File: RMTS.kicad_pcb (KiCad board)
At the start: 2 copper layers, 78.1 x 50.2 mm, 79 parts, among them J1 USB_B_Mini, J10 CONN_02, J11 CONN_02, J12 CONN_02, J2 Programmer, J3 Screw_Terminal_01x03, J4 Screw_Terminal_01x04, J5 Screw_Terminal_01x02, J6 Screw_Terminal_01x02, J7 Micro_SD_Card_Det_Hirose_DM3AT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

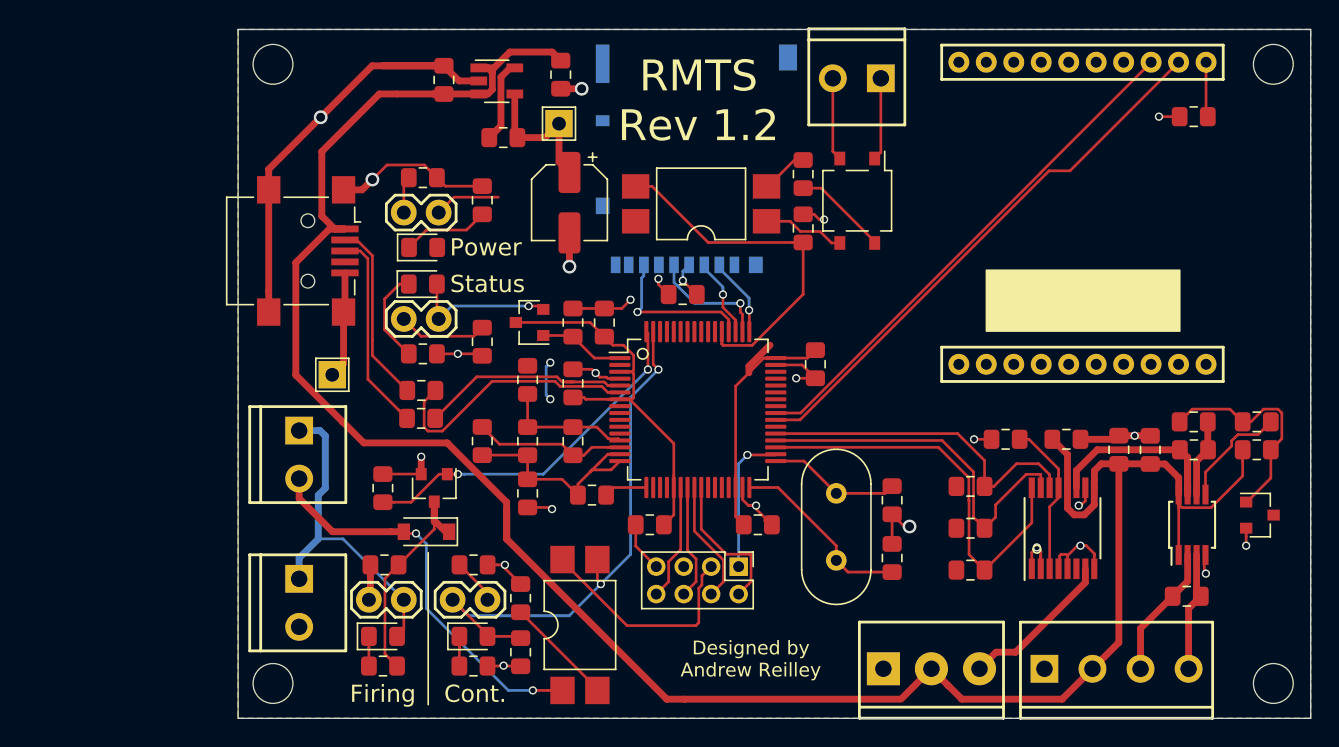
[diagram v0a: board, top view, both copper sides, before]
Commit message: Update programmer header, remove USB port
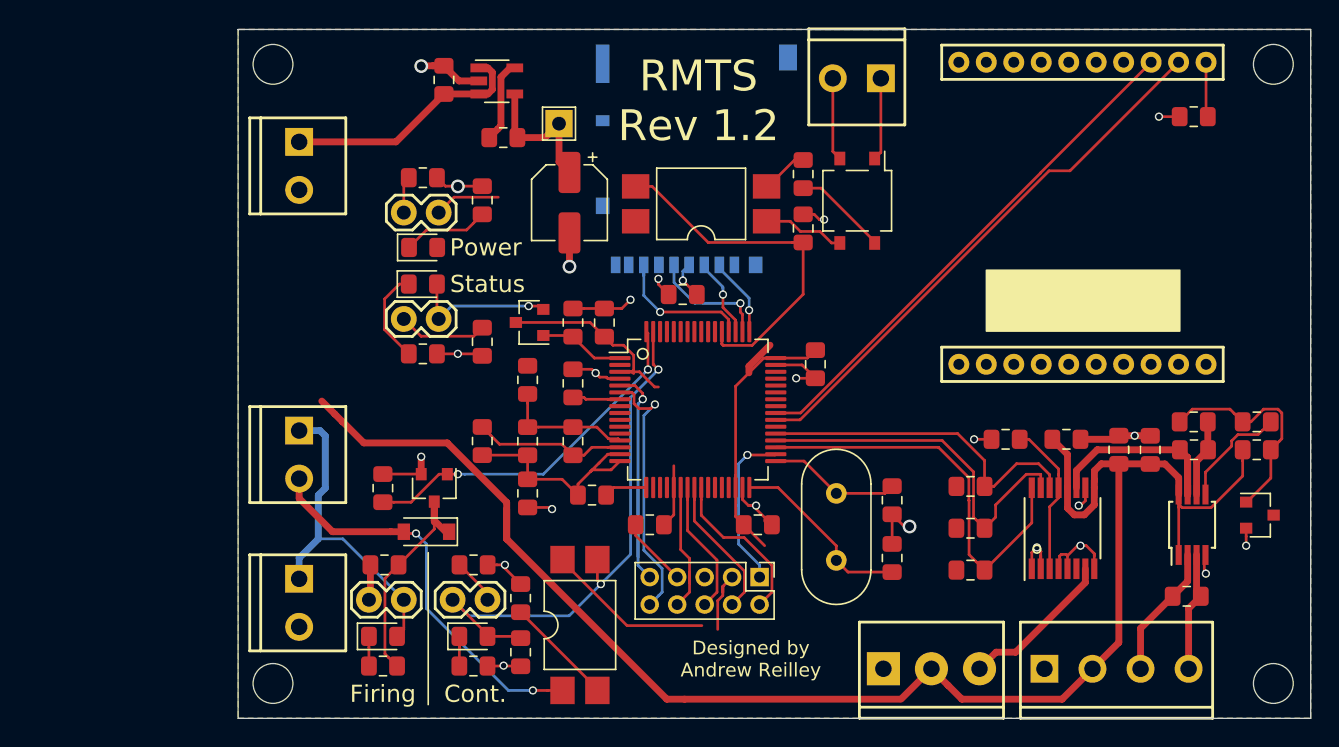
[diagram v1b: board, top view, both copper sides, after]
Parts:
- removed R1, R2: 33, Resistor_SMD:R_0805_2012Metric_Pad1.15x1.40mm_HandSolder
- removed R13: 330, Resistor_SMD:R_0805_2012Metric_Pad1.15x1.40mm_HandSolder
- removed TP1: GND, TestPoint:TestPoint_THTPad_2.0x2.0mm_Drill1.0mm
- J1: value USB_B_Mini -> Screw_Terminal_01x02; footprint Connector_USB:USB_Mini-B_Lumberg_2486_01_Horizontal -> Connectors:SCREWTERMINAL-3.5MM-2
- J2: footprint Connector_PinHeader_2.00mm:PinHeader_2x04_P2.00mm_Vertical -> Connector_PinHeader_2.00mm:PinHeader_2x05_P2.00mm_Vertical
- moved J1 7.97 mm to (136.5, 70.4)
- moved J2 1.70 mm to (170.1, 102.1)
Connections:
- C1 pad 1: /VBUS -> Net-(C1-Pad1)
- J1 pad 1: /VBUS -> Net-(C1-Pad1)
- J1 pad 2: Net-(J1-Pad2) -> GND
- U1 pad 1: /VBUS -> Net-(C1-Pad1)
- U1 pad 3: /VBUS -> Net-(C1-Pad1)
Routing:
- net /VBUS: track 165.2 -> 118.3 mm
- net GND: track 123.5 -> 78.6 mm, vias 24 -> 23
- net Net-(C1-Pad1): track 0.00 -> 18.0 mm
- net Net-(J1-Pad3): track 14.7 -> 0.00 mm
- net Net-(J1-Pad2): track 13.3 -> 0.00 mm
- net +3V3: track 102.9 -> 96.8 mm, vias 3 -> 1
- net /USBP: track 15.6 -> 20.8 mm, vias 0 -> 1
- net /PTA0: track 8.50 -> 9.96 mm
- net /RST: track 10.5 -> 11.9 mm
- net /PTA2: track 9.01 -> 10.4 mm
- net /PTA1: track 8.39 -> 9.79 mm
- net /PTA3: track 10.7 -> 11.9 mm
- net /SD_DO: track 11.4 -> 10.8 mm
- net /USBM: track 19.2 -> 19.4 mm, vias 0 -> 1

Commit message: Added 5v reg, broke layout
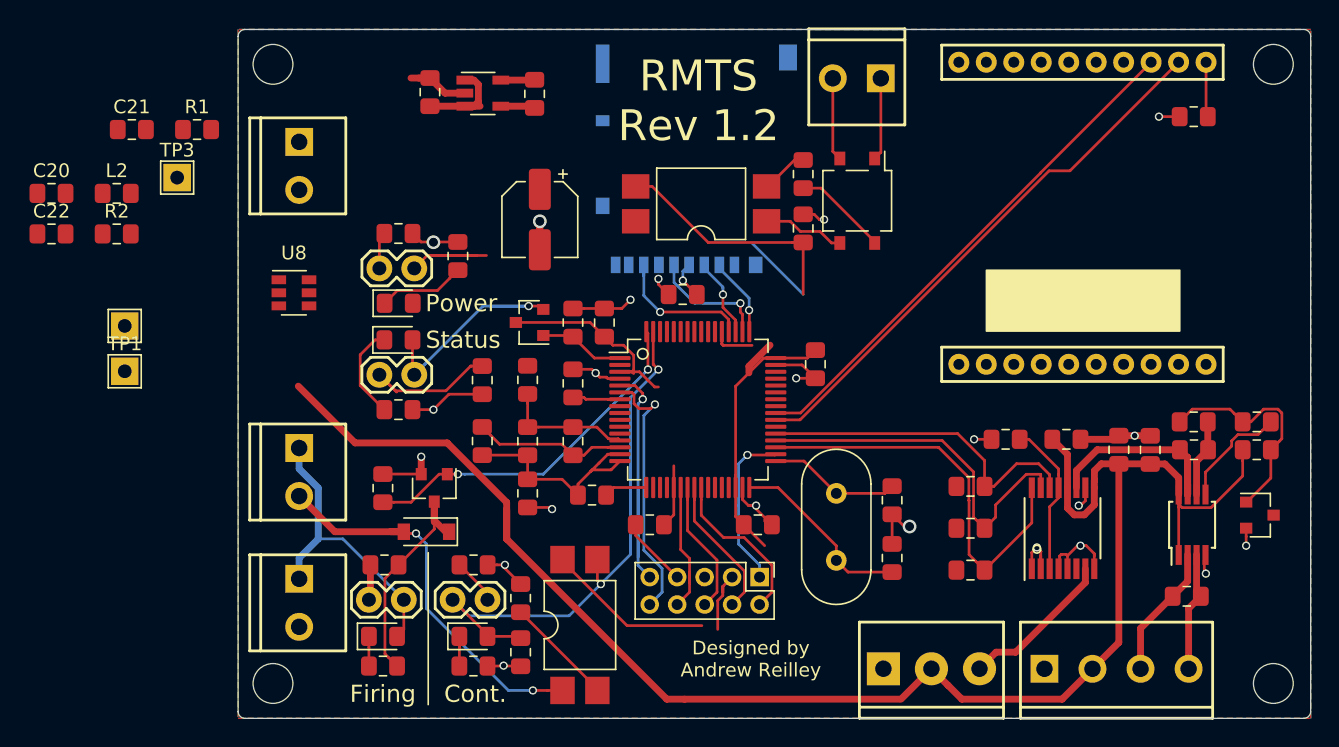
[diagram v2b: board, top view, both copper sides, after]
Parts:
- added C20: 2.2uF, Capacitor_SMD:C_0805_2012Metric_Pad1.15x1.40mm_HandSolder, F.Cu at (118.5, 74.2)
- added C21: 0.1uF, Capacitor_SMD:C_0805_2012Metric_Pad1.15x1.40mm_HandSolder, F.Cu at (124.3, 69.5)
- added C22: 10uF, Capacitor_SMD:C_0805_2012Metric_Pad1.15x1.40mm_HandSolder, F.Cu at (118.5, 77.1)
- added L2: 4.7uH, Inductor_SMD:L_0805_2012Metric_Pad1.15x1.40mm_HandSolder, F.Cu at (123.2, 74.2)
- added R1: 88.7k, Resistor_SMD:R_0805_2012Metric_Pad1.15x1.40mm_HandSolder, F.Cu at (129.1, 69.5)
- added R2: 22.1k, Resistor_SMD:R_0805_2012Metric_Pad1.15x1.40mm_HandSolder, F.Cu at (123.2, 77.1)
- added TP1: GND, TestPoint:TestPoint_THTPad_2.0x2.0mm_Drill1.0mm, F.Cu at (123.8, 87.1)
- added TP3: 5V, TestPoint:TestPoint_THTPad_2.0x2.0mm_Drill1.0mm, F.Cu at (127.6, 73.0)
- added U8: LMR50410-Q1, Package_TO_SOT_SMD:SOT-23-6, F.Cu at (136.1, 81.4)
- moved TP2 34.9 mm to (123.8, 83.8)
- moved J11 4.44 mm to (144.9, 79.6)
- moved J12 4.44 mm to (144.9, 87.4)
- moved R16 4.44 mm to (148.1, 78.7)
- moved D5 4.44 mm to (143.8, 82.2)
- moved D6 4.44 mm to (143.8, 84.8)
- moved R17 4.44 mm to (143.8, 89.9)
- moved R19 4.44 mm to (143.8, 77.1)
- moved L1 3.91 mm to (153.7, 66.9), turned to 270 degrees
- moved R21 2.79 mm to (149.9, 87.8)
- moved C2 2.48 mm to (154.1, 76.1)
- moved C1 1.35 mm to (146.1, 66.8)
- moved U1 1.35 mm to (149.9, 66.9)
- moved J6 1.27 mm to (136.5, 92.7)
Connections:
- C1 pad 1: Net-(C1-Pad1) -> +5V
- C11 pad 1: /VBUS -> +5V
- C18 pad 1: /VBUS -> +5V
- C19 pad 1: /VBUS -> +5V
- J1 pad 1: Net-(C1-Pad1) -> Net-(C20-Pad1)
- J3 pad 2: /VBUS -> +5V
- J4 pad 2: /VBUS -> +5V
- R25 pad 1: /VBUS -> +5V
- U1 pad 1: Net-(C1-Pad1) -> +5V
- U1 pad 3: Net-(C1-Pad1) -> +5V
- U3 pad 10: GND -> Net-(U3-Pad10)
- U3 pad 12: /VBUS -> +5V
- U3 pad 9: /VBUS -> +5V
- U4 pad 1: /VBUS -> +5V
- U4 pad 8: /VBUS -> +5V
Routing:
- net +5V: track 0.00 -> 127.7 mm
- net /VBUS: track 118.3 -> 0.00 mm
- net Net-(C1-Pad1): track 18.0 -> 0.00 mm
- net Net-(D6-Pad2): track 10.9 -> 18.5 mm
- net GND: track 78.6 -> 84.3 mm, vias 23 -> 21
- net /EXT_FIRE: track 26.1 -> 20.8 mm
- net Net-(J12-Pad2): track 6.49 -> 10.5 mm
- net +3V3: track 96.8 -> 93.2 mm
- net Net-(L1-Pad1): track 6.04 -> 2.81 mm
- net Net-(D1-Pad2): track 26.2 -> 23.6 mm
- net Net-(U3-Pad10): track 0.00 -> 1.58 mm, vias 0 -> 1
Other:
- outline, holes or cut-outs redrawn

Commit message: Fixed layout of new 5v regulator
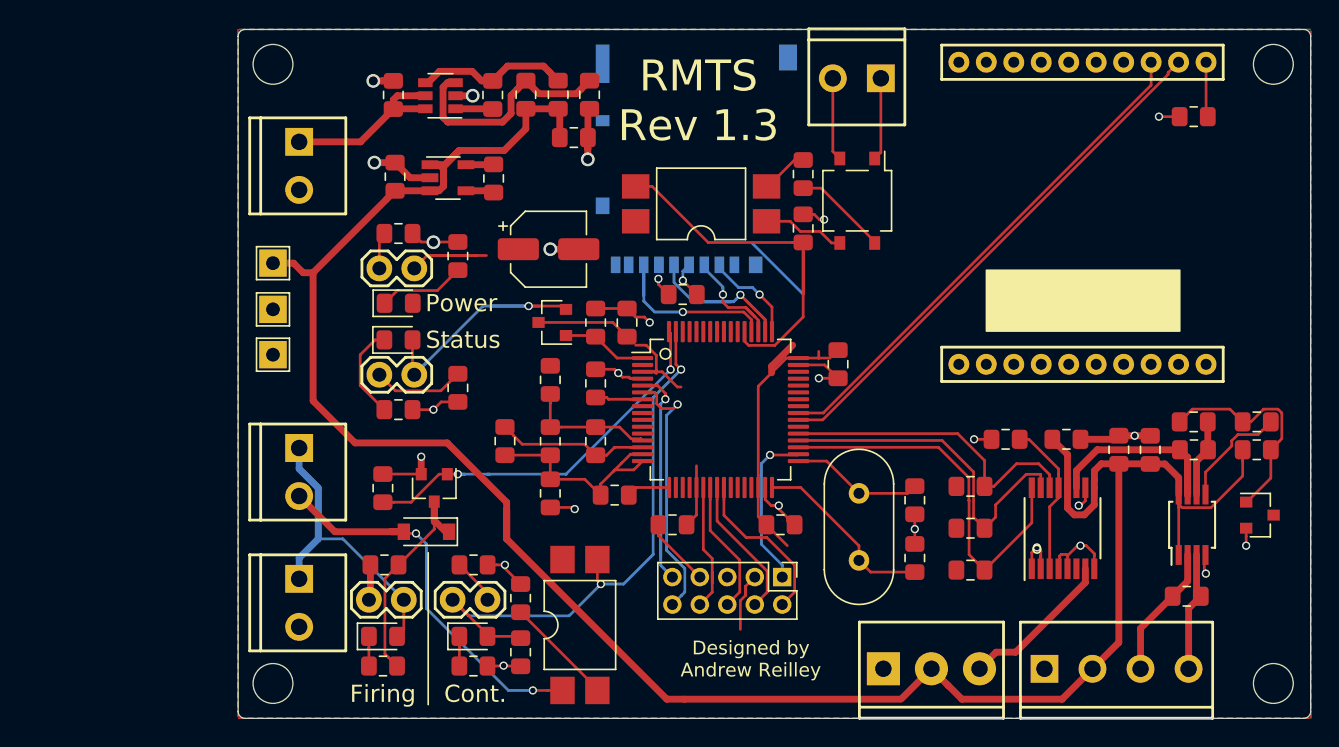
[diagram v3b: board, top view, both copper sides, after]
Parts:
- moved C22 38.7 mm to (156.5, 70.1)
- moved R2 35.9 mm to (157.7, 67.0), turned to 270 degrees
- moved L2 32.9 mm to (155.4, 67.0), turned to 270 degrees
- moved C21 26.4 mm to (150.6, 67.0), turned to 90 degrees
- moved C20 25.9 mm to (143.4, 67.0), turned to 90 degrees
- moved R1 24.1 mm to (153.0, 67.0), turned to 90 degrees
- moved U8 17.9 mm to (146.8, 67.1), turned to 180 degrees
- moved TP1 10.9 mm to (134.6, 85.9)
- moved TP2 10.9 mm to (134.6, 82.6)
- moved TP3 9.36 mm to (134.6, 79.2)
- moved L1 6.84 mm to (150.7, 73.1)
- moved U1 6.66 mm to (147.4, 73.0)
- moved C1 6.66 mm to (143.5, 73.0)
- moved C2 2.25 mm to (154.7, 78.2), turned to 0 degrees
- moved R21 1.86 mm to (148.1, 88.3)
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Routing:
- net +5V: track 127.7 -> 163.2 mm
- net Net-(R1-Pad2): track 0.00 -> 16.9 mm
- net Net-(C20-Pad1): track 0.00 -> 13.9 mm
- net +3V3: track 93.2 -> 79.7 mm
- net Net-(C21-Pad2): track 0.00 -> 11.2 mm
- net /SD_CLK: track 8.88 -> 17.7 mm
- net /EXT_FIRE: track 20.8 -> 28.4 mm
- net /SD_DO: track 10.8 -> 14.9 mm
- net Net-(J12-Pad2): track 10.5 -> 7.52 mm
- net Net-(C21-Pad1): track 0.00 -> 2.72 mm
- net Net-(D6-Pad2): track 18.5 -> 21.0 mm
- net /SD_DI: track 5.81 -> 8.18 mm
- net /Fire: track 26.1 -> 28.4 mm
- net GND: track 84.3 -> 86.4 mm, vias 21 -> 25
- net /ASDA: track 27.0 -> 25.3 mm
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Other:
- board text added: "RMTS Rev 1.3"
- board text removed: "RMTS Rev 1.2"

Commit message: Upgrade firing diode
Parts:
- D3: footprint Diode_SMD:D_SOD-123 -> Diode_SMD:D_SMA
- moved Q1 2.25 mm to (144.8, 94.0)
- moved R18 1.88 mm to (141.7, 94.0)
- moved D3 0.52 mm to (145.7, 98.3)
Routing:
- net Net-(D1-Pad2): track 23.6 -> 26.8 mm
- net /Fire: track 28.4 -> 30.8 mm
- net Net-(D3-Pad1): track 16.6 -> 18.5 mm
- net +5V: track 163.2 -> 161.5 mm
- net Net-(D3-Pad2): track 28.8 -> 27.8 mm
- net GND: track 86.4 -> 85.6 mm
- net +3V3: track 79.7 -> 78.9 mm

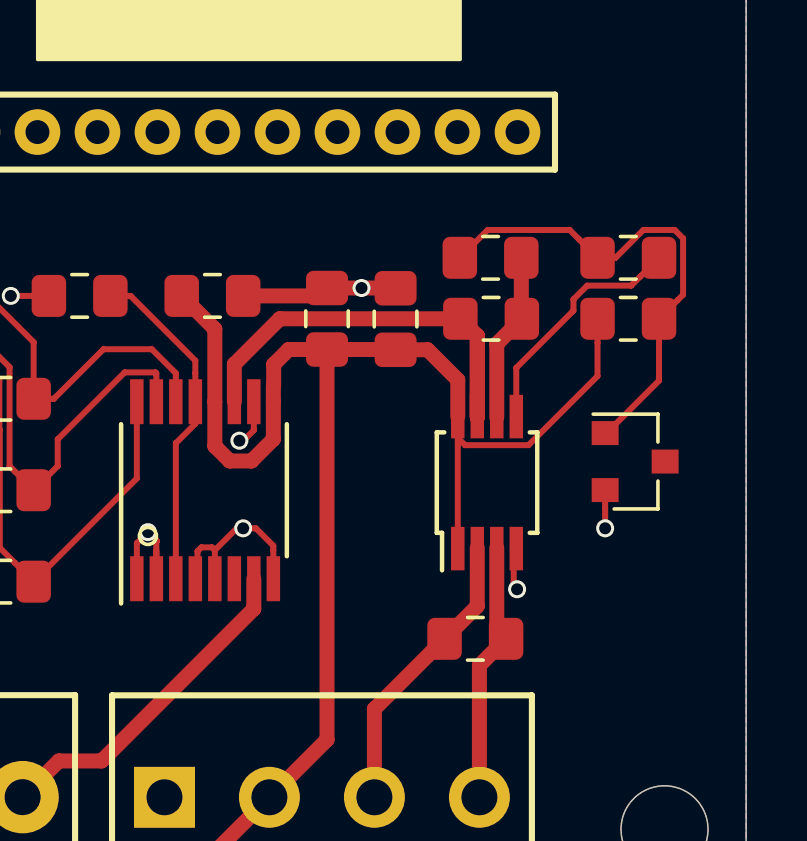
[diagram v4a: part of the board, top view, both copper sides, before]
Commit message: Added test points
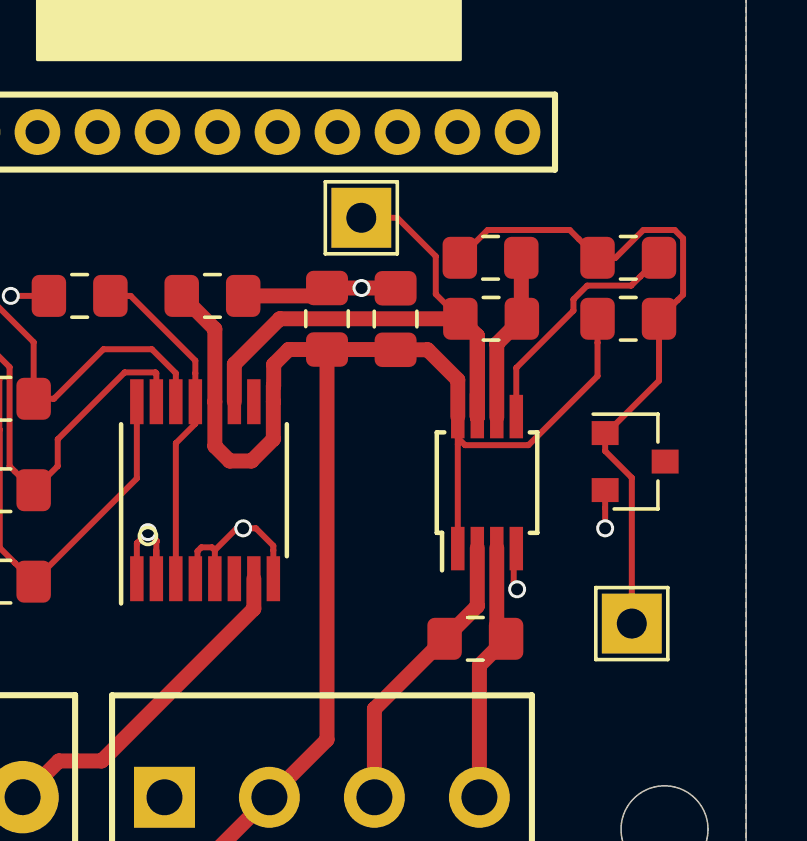
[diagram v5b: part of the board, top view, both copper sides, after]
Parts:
- added TP4: 5V, TestPoint:TestPoint_THTPad_2.0x2.0mm_Drill1.0mm, F.Cu at (206.4, 103.0)
- added TP5: 5V, TestPoint:TestPoint_THTPad_2.0x2.0mm_Drill1.0mm, F.Cu at (197.4, 89.5)
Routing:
- net Net-(R24-Pad2): track 16.3 -> 23.0 mm
- net /LC0: track 16.4 -> 21.8 mm
- net Net-(U3-Pad10): track 1.58 -> 0.00 mm, vias 1 -> 0
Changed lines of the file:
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@@
     (thickness 1.6)
     (drawings 33)
-    (tracks 652)
+    (tracks 656)
     (zones 0)
-    (modules 84)
+    (modules 86)
     (nets 111)
   )
@@
     (uvia_drill 0.1)
   )
+  (module TestPoint:TestPoint_THTPad_2.0x2.0mm_Drill1.0mm (layer F.Cu)
+    (at 197.358 89.4715)
+    (descr "THT rectangular pad as test Point, square 2.0mm_Drill1.0mm  side length, hole diameter 1.0mm")
+    (tags "test point THT pad rectangle square")
+    (attr virtual)
+    (fp_text reference TP5 (at -3.1115 0) (layer F.SilkS) hide
+      (effects (font (size 1 1) (thickness 0.15)))
+    )
+    (fp_text value 5V (at 0 2.05) (layer F.Fab)
+      (effects (font (size 1 1) (thickness 0.15)))
+    )
+    (fp_line (start 1.5 1.5) (end -1.5 1.5) (layer F.CrtYd) (width 0.05))
+    (fp_line (start 1.5 1.5) (end 1.5 -1.5) (layer F.CrtYd) (width 0.05))
+    (fp_line (start -1.5 -1.5) (end -1.5 1.5) (layer F.CrtYd) (width 0.05))
+    (fp_line (start -1.5 -1.5) (end 1.5 -1.5) (layer F.CrtYd) (width 0.05))
+    (fp_line (start -1.2 1.2) (end -1.2 -1.2) (layer F.SilkS) (width 0.12))
+    (fp_line (start 1.2 1.2) (end -1.2 1.2) (layer F.SilkS) (width 0.12))
+    (fp_line (start 1.2 -1.2) (end 1.2 1.2) (layer F.SilkS) (width 0.12))
+    (fp_line (start -1.2 -1.2) (end 1.2 -1.2) (layer F.SilkS) (width 0.12))
+    (fp_text user %R (at 0 -2) (layer F.Fab)
+      (effects (font (size 1 1) (thickness 0.15)))
+    )
+    (pad 1 thru_hole rect (at 0 0) (size 2 2) (drill 1) (layers *.Cu *.Mask)
+      (net 42 /LC0))
+  )
+  (module TestPoint:TestPoint_THTPad_2.0x2.0mm_Drill1.0mm (layer F.Cu)
+    (at 206.375 102.997)
+    (descr "THT rectangular pad as test Point, square 2.0mm_Drill1.0mm  side length, hole diameter 1.0mm")
+    (tags "test point THT pad rectangle square")
+    (attr virtual)
+    (fp_text reference TP4 (at 0 -1.998) (layer F.SilkS) hide
+      (effects (font (size 1 1) (thickness 0.15)))
+    )
+    (fp_text value 5V (at 0 2.05) (layer F.Fab)
+      (effects (font (size 1 1) (thickness 0.15)))
+    )
+    (fp_line (start 1.5 1.5) (end -1.5 1.5) (layer F.CrtYd) (width 0.05))
+    (fp_line (start 1.5 1.5) (end 1.5 -1.5) (layer F.CrtYd) (width 0.05))
+    (fp_line (start -1.5 -1.5) (end -1.5 1.5) (layer F.CrtYd) (width 0.05))
+    (fp_line (start -1.5 -1.5) (end 1.5 -1.5) (layer F.CrtYd) (width 0.05))
+    (fp_line (start -1.2 1.2) (end -1.2 -1.2) (layer F.SilkS) (width 0.12))
+    (fp_line (start 1.2 1.2) (end -1.2 1.2) (layer F.SilkS) (width 0.12))
+    (fp_line (start 1.2 -1.2) (end 1.2 1.2) (layer F.SilkS) (width 0.12))
+    (fp_line (start -1.2 -1.2) (end 1.2 -1.2) (layer F.SilkS) (width 0.12))
+    (fp_text user %R (at 0 -2) (layer F.Fab)
+      (effects (font (size 1 1) (thickness 0.15)))
+    )
+    (pad 1 thru_hole rect (at 0 0) (size 2 2) (drill 1) (layers *.Cu *.Mask)
+      (net 103 "Net-(R24-Pad2)"))
+  )
   (module Diode_SMD:D_SMA (layer F.Cu)
     (at 145.669 98.298 180)
@@
   (segment (start 201.224 96.098) (end 201.224 93.401) (width 0.5) (layer F.Cu) (net 42))
   (segment (start 200.66 92.837) (end 194.641 92.837) (width 0.5) (layer F.Cu) (net 42))
+  (segment (start 198.558 89.4715) (end 197.358 89.4715) (width 0.2) (layer F.Cu) (net 42))
+  (segment (start 199.83999 90.75349) (end 198.558 89.4715) (width 0.2) (layer F.Cu) (net 42))
+  (segment (start 199.83999 92.01699) (end 199.83999 90.75349) (width 0.2) (layer F.Cu) (net 42))
+  (segment (start 200.66 92.837) (end 199.83999 92.01699) (width 0.2) (layer F.Cu) (net 42))
   (segment (start 185.812628 97.928628) (end 186.436 98.552) (width 0.2) (layer F.Cu) (net 43))
   (segment (start 185.63399 97.74999) (end 185.812628 97.928628) (width 0.2) (layer F.Cu) (net 43))
@@
   (segment (start 207.282 94.901) (end 205.536 96.647) (width 0.2) (layer F.Cu) (net 103))
   (segment (start 207.282 92.837) (end 207.282 94.901) (width 0.2) (layer F.Cu) (net 103))
+  (segment (start 206.375 101.797) (end 206.375 102.997) (width 0.2) (layer F.Cu) (net 103))
+  (segment (start 206.375 98.136) (end 206.375 101.797) (width 0.2) (layer F.Cu) (net 103))
+  (segment (start 205.486 97.247) (end 206.375 98.136) (width 0.2) (layer F.Cu) (net 103))
+  (segment (start 205.486 96.647) (end 205.486 97.247) (width 0.2) (layer F.Cu) (net 103))
   (segment (start 202.524 95.717) (end 202.565 95.676) (width 0.2) (layer F.Cu) (net 104))
   (segment (start 202.524 96.123) (end 202.524 95.717) (width 0.2) (layer F.Cu) (net 104))
@@
   (segment (start 153.98701 66.91051) (end 156.71849 66.91051) (width 0.5) (layer F.Cu) (net 109))
   (segment (start 153.035 65.9585) (end 153.98701 66.91051) (width 0.5) (layer F.Cu) (net 109))
-  (via (at 193.294 96.901) (size 0.6) (drill 0.4) (layers F.Cu B.Cu) (net 110))
-  (segment (start 193.776 95.602) (end 193.776 96.552) (width 0.2) (layer F.Cu) (net 110))
-  (segment (start 193.427 96.901) (end 193.294 96.901) (width 0.2) (layer F.Cu) (net 110))
-  (segment (start 193.776 96.552) (end 193.427 96.901) (width 0.2) (layer F.Cu) (net 110))
   (zone (net 1) (net_name GND) (layer B.Cu) (hatch edge 0.508)
     (connect_pads (clearance 0.508))
